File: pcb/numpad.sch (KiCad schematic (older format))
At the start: 32 parts, among them CON1 ISP, J1 USB-MINI-B, SW1 NUMLOCK, SW10 *, SW11 9, SW12 6, SW13 3, SW14 ., SW15 -, SW16 +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

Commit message: version that was milled at school
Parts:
- added P1, P2, P3, P4, P5, P6: CONN_1, symbol CONN_1
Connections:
- net GND: now also P1.1, P2.1, P3.1, P4.1, P5.1, P6.1

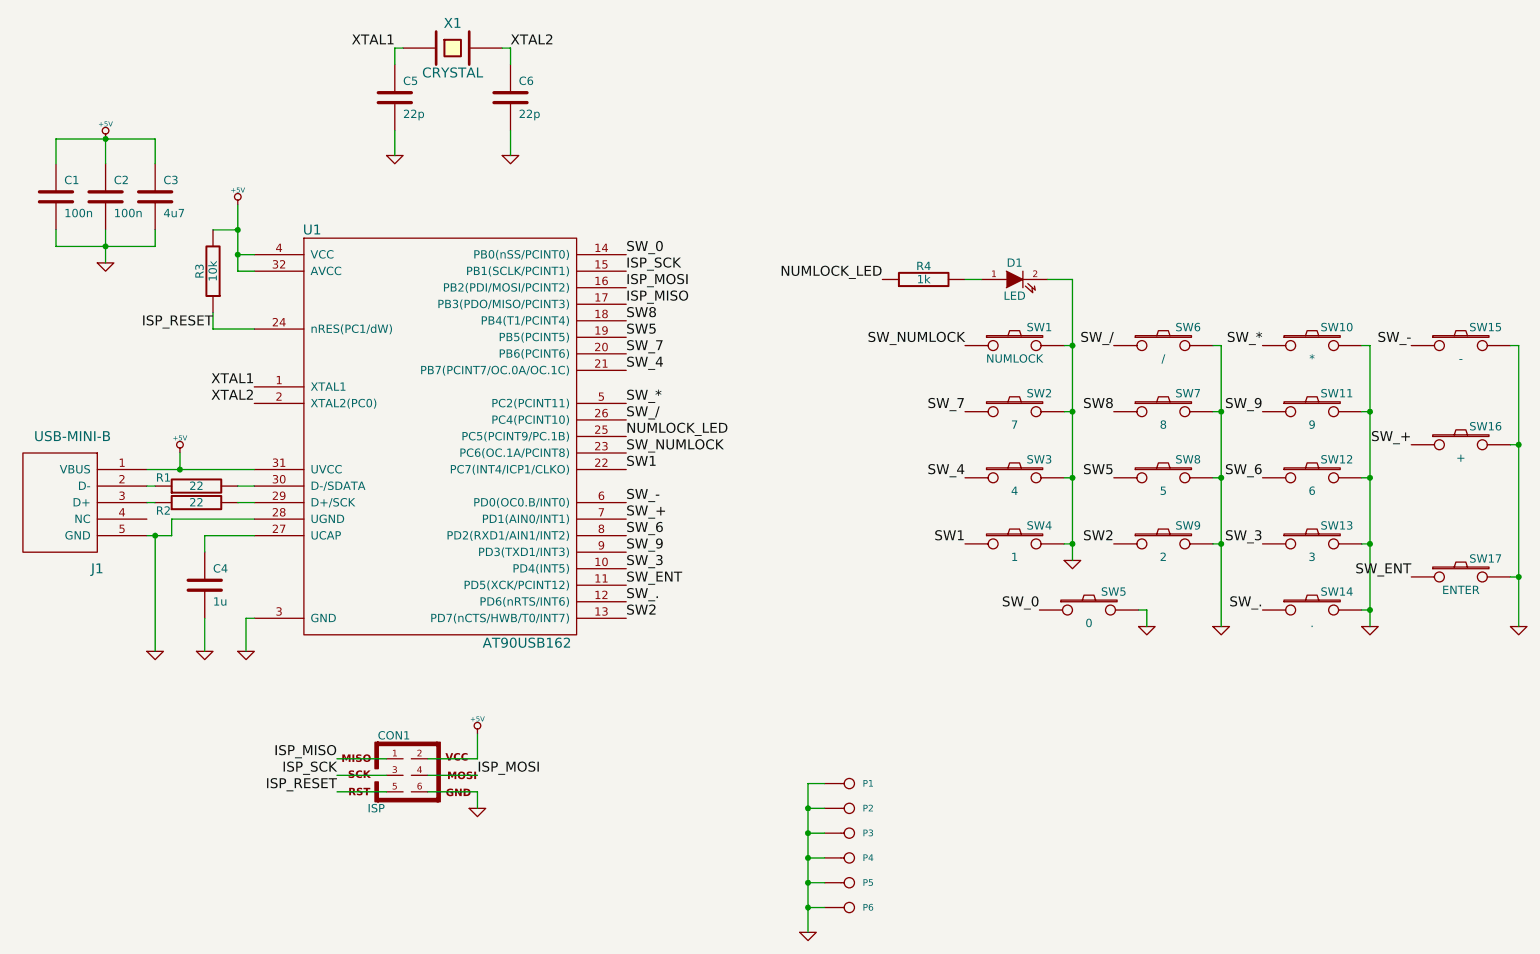
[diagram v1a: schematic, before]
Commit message: moved silkscreen labels around
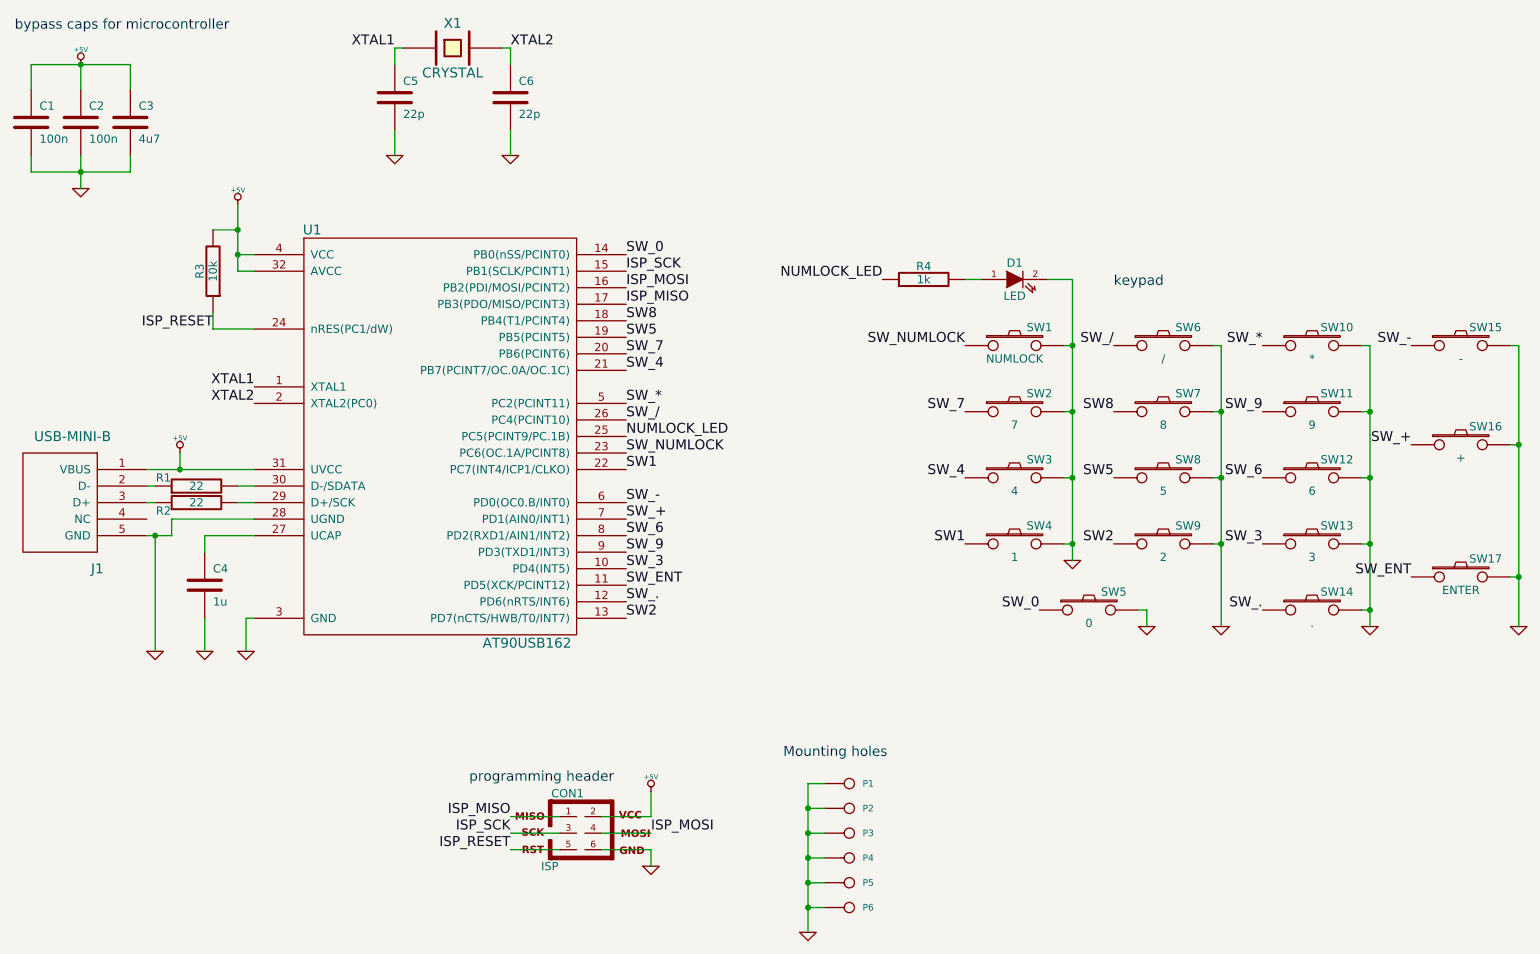
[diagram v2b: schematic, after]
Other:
- note added: "Mounting holes"
- note added: "bypass caps for microcontroller"
- note added: "keypad"
- note added: "programming header"
- moved on the sheet: C1, C2, C3, CON1
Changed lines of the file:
@@
-EESchema Schematic File Version 2  date Wed 12 Sep 2012 07:57:32 PM EEST
+EESchema Schematic File Version 2  date to 13. syyskuuta 2012 16.19.21
 LIBS:power
 LIBS:device
@@
 EELAYER 25  0
 EELAYER END
-$Descr A4 11700 8267
+$Descr A4 11693 8268
 encoding utf-8
 Sheet 1 1
-Title ""
-Date "12 sep 2012"
-Rev ""
-Comp ""
+Title "USB Cherry Numpad"
+Date "13 sep 2012"
+Rev "1"
+Comp "Tuomas Nylund"
 Comment1 ""
 Comment2 ""
@@
 Connection ~ 2050 2150
 Wire Wire Line
-	1250 2000 1250 2200
-Wire Wire Line
-	950  2100 1550 2100
-Wire Wire Line
-	950  2100 950  2000
-Wire Wire Line
-	1550 2100 1550 2000
-Connection ~ 1250 2100
-Wire Wire Line
-	950  1450 1550 1450
-Wire Wire Line
-	950  1450 950  1600
-Wire Wire Line
-	1250 1450 1250 1600
-Wire Wire Line
-	1550 1450 1550 1600
+	1100 1550 1100 1750
+Wire Wire Line
+	800  1650 1400 1650
+Wire Wire Line
+	800  1650 800  1550
+Wire Wire Line
+	1400 1650 1400 1550
+Connection ~ 1100 1650
+Wire Wire Line
+	800  1000 1400 1000
+Wire Wire Line
+	800  1000 800  1150
+Wire Wire Line
+	1100 1000 1100 1150
+Wire Wire Line
+	1400 1000 1400 1150
 Wire Wire Line
 	3700 1550 3700 1400
@@
 Connection ~ 9800 4100
 Wire Wire Line
-	3500 5050 3500 5200
-Wire Wire Line
-	3500 5200 3200 5200
-Wire Wire Line
-	3500 5300 3200 5300
-Wire Wire Line
-	3200 5400 3500 5400
-Wire Wire Line
-	3500 5400 3500 5500
-Wire Wire Line
-	2950 5400 2650 5400
-Wire Wire Line
-	2650 5300 2950 5300
-Wire Wire Line
-	2950 5200 2650 5200
-Connection ~ 1250 1450
+	4550 5400 4550 5550
+Wire Wire Line
+	4550 5550 4250 5550
+Wire Wire Line
+	4550 5650 4250 5650
+Wire Wire Line
+	4250 5750 4550 5750
+Wire Wire Line
+	4550 5750 4550 5850
+Wire Wire Line
+	4000 5750 3700 5750
+Wire Wire Line
+	3700 5650 4000 5650
+Wire Wire Line
+	4000 5550 3700 5550
+Connection ~ 1100 1000
 Wire Wire Line
 	5500 6250 5500 5350
@@
 L AVR-ISP-6 CON1
 U 1 1 504F6B93
-P 3075 5300
-F 0 "CON1" H 2995 5540 50  0000 C CNN
-F 1 "ISP" H 2835 5070 50  0000 L BNN
-F 2 "AVR-ISP-6" V 2555 5340 50  0001 C CNN
-	1    3075 5300
+P 4125 5650
+F 0 "CON1" H 4045 5890 50  0000 C CNN
+F 1 "ISP" H 3885 5420 50  0000 L BNN
+F 2 "AVR-ISP-6" V 3605 5690 50  0001 C CNN
+	1    4125 5650
 	1    0    0    -1
 $EndComp
@@
 L C C1
 U 1 1 504F707A
-P 950 1800
-F 0 "C1" H 1000 1900 50  0000 L CNN
-F 1 "100n" H 1000 1700 50  0000 L CNN
-	1    950  1800
+P 800 1350
+F 0 "C1" H 850 1450 50  0000 L CNN
+F 1 "100n" H 850 1250 50  0000 L CNN
+	1    800  1350
 	1    0    0    -1
 $EndComp
@@
 L C C2
 U 1 1 504F7087
-P 1250 1800
-F 0 "C2" H 1300 1900 50  0000 L CNN
-F 1 "100n" H 1300 1700 50  0000 L CNN
-	1    1250 1800
+P 1100 1350
+F 0 "C2" H 1150 1450 50  0000 L CNN
+F 1 "100n" H 1150 1250 50  0000 L CNN
+	1    1100 1350
 	1    0    0    -1
 $EndComp
@@
 L C C3
 U 1 1 504F7097
-P 1550 1800
-F 0 "C3" H 1600 1900 50  0000 L CNN
-F 1 "4u7" H 1600 1700 50  0000 L CNN
-	1    1550 1800
+P 1400 1350
+F 0 "C3" H 1450 1450 50  0000 L CNN
+F 1 "4u7" H 1450 1250 50  0000 L CNN
+	1    1400 1350
 	1    0    0    -1
 $EndComp
@@
 L GND #PWR07
 U 1 1 504F70A4
-P 1250 2200
-F 0 "#PWR07" H 1250 2200 30  0001 C CNN
-F 1 "GND" H 1250 2130 30  0001 C CNN
-	1    1250 2200
+P 1100 1750
+F 0 "#PWR07" H 1100 1750 30  0001 C CNN
+F 1 "GND" H 1100 1680 30  0001 C CNN
+	1    1100 1750
 	1    0    0    -1
 $EndComp
@@
 L +5V #PWR08
 U 1 1 504F70FF
-P 1250 1450
-F 0 "#PWR08" H 1250 1540 20  0001 C CNN
-F 1 "+5V" H 1250 1540 30  0000 C CNN
-	1    1250 1450
+P 1100 1000
+F 0 "#PWR08" H 1100 1090 20  0001 C CNN
+F 1 "+5V" H 1100 1090 30  0000 C CNN
+	1    1100 1000
 	1    0    0    -1
 $EndComp
@@
 	1    0    0    -1
 $EndComp
-Text Label 3500 5300 0    60   ~ 0
+Text Label 4550 5650 0    60   ~ 0
 ISP_MOSI
-Text Label 2650 5200 2    60   ~ 0
+Text Label 3700 5550 2    60   ~ 0
 ISP_MISO
-Text Label 2650 5300 2    60   ~ 0
+Text Label 3700 5650 2    60   ~ 0
 ISP_SCK
-Text Label 2650 5400 2    60   ~ 0
+Text Label 3700 5750 2    60   ~ 0
 ISP_RESET
 $Comp
 L GND #PWR016
 U 1 1 504F7B05
-P 3500 5500
-F 0 "#PWR016" H 3500 5500 30  0001 C CNN
-F 1 "GND" H 3500 5430 30  0001 C CNN
-	1    3500 5500
+P 4550 5850
+F 0 "#PWR016" H 4550 5850 30  0001 C CNN
+F 1 "GND" H 4550 5780 30  0001 C CNN
+	1    4550 5850
 	1    0    0    -1
 $EndComp
@@
 L +5V #PWR017
 U 1 1 504F7B0B
-P 3500 5050
-F 0 "#PWR017" H 3500 5140 20  0001 C CNN
-F 1 "+5V" H 3500 5140 30  0000 C CNN
-	1    3500 5050
+P 4550 5400
+F 0 "#PWR017" H 4550 5490 20  0001 C CNN
+F 1 "+5V" H 4550 5490 30  0000 C CNN
+	1    4550 5400
 	1    0    0    -1
 $EndComp
@@
 Text Label 5950 2300 2    60   ~ 0
 NUMLOCK_LED
+Text Notes 5350 5200 0    60   ~ 0
+Mounting holes
+Text Notes 3450 5350 0    60   ~ 0
+programming header
+Text Notes 7350 2350 0    60   ~ 0
+keypad
+Text Notes 700  800  0    60   ~ 0
+bypass caps for microcontroller
 $EndSCHEMATC

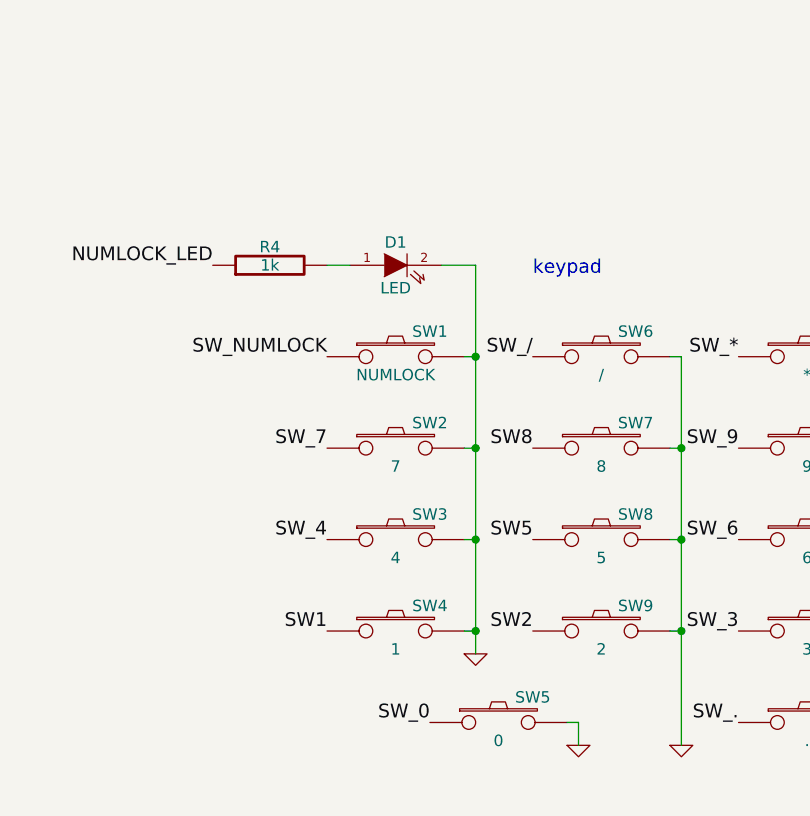
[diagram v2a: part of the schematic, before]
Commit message: added second LED footprint for capslock inside switch
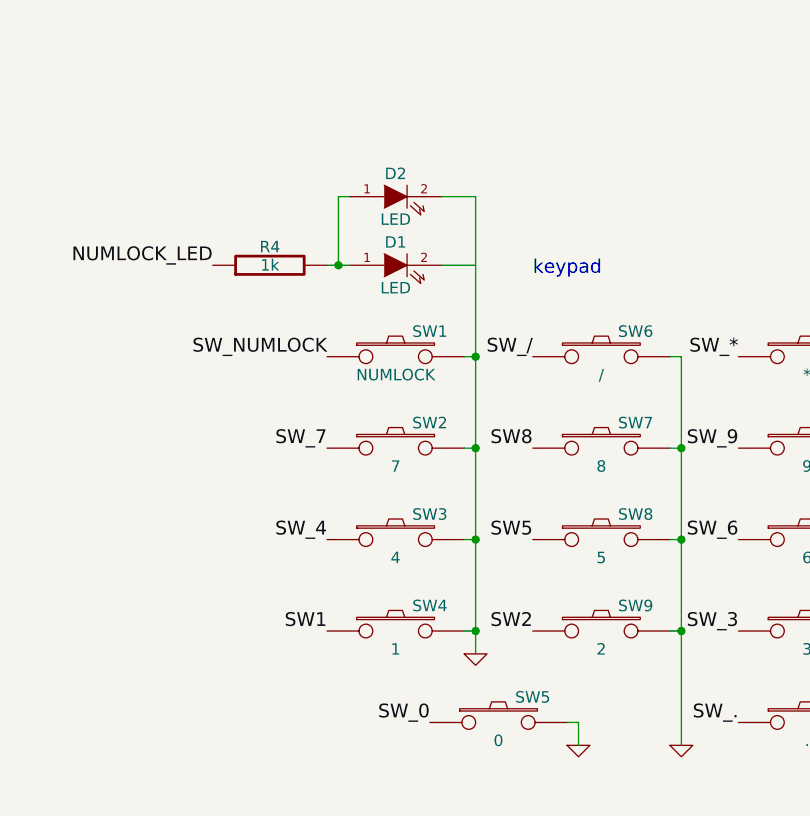
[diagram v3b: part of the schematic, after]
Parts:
- added D2: LED, symbol LED
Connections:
- net GND: now also D2.2 (K); no longer D1.2 (K)
- net at D1.1 (A), R4.2: now also D2.1 (A)
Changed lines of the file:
@@
-EESchema Schematic File Version 2  date to 13. syyskuuta 2012 16.19.21
+EESchema Schematic File Version 2  date pe 14. syyskuuta 2012 11.25.54
 LIBS:power
 LIBS:device
@@
 Sheet 1 1
 Title "USB Cherry Numpad"
-Date "13 sep 2012"
+Date "14 sep 2012"
 Rev "1"
 Comp "Tuomas Nylund"
@@
 	6450 2300 6550 2300
 Wire Wire Line
-	7100 4000 7100 2300
+	7100 2000 7100 4000
 Wire Wire Line
 	7100 2300 6950 2300
@@
 Text Notes 700  800  0    60   ~ 0
 bypass caps for microcontroller
+$Comp
+L LED D2
+U 1 1 5052EB74
+P 6750 2000
+F 0 "D2" H 6750 2100 50  0000 C CNN
+F 1 "LED" H 6750 1900 50  0000 C CNN
+	1    6750 2000
+	1    0    0    -1
+$EndComp
+Wire Wire Line
+	6950 2000 7100 2000
+Wire Wire Line
+	6500 2300 6500 2000
+Wire Wire Line
+	6500 2000 6550 2000
+Connection ~ 6500 2300
 $EndSCHEMATC
